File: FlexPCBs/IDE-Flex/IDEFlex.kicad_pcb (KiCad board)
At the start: 2 copper layers, 106.1 x 55.1 mm, 18 parts, among them J1 Conn_01x04_Pin, J2 Conn_01x04_Pin, J3 Conn_01x04_Pin, J4 Conn_01x04_Pin, J5 Conn_01x04_Pin, J6 Conn_01x04_Pin, J7 Conn_01x04_Pin, U1 IDE25

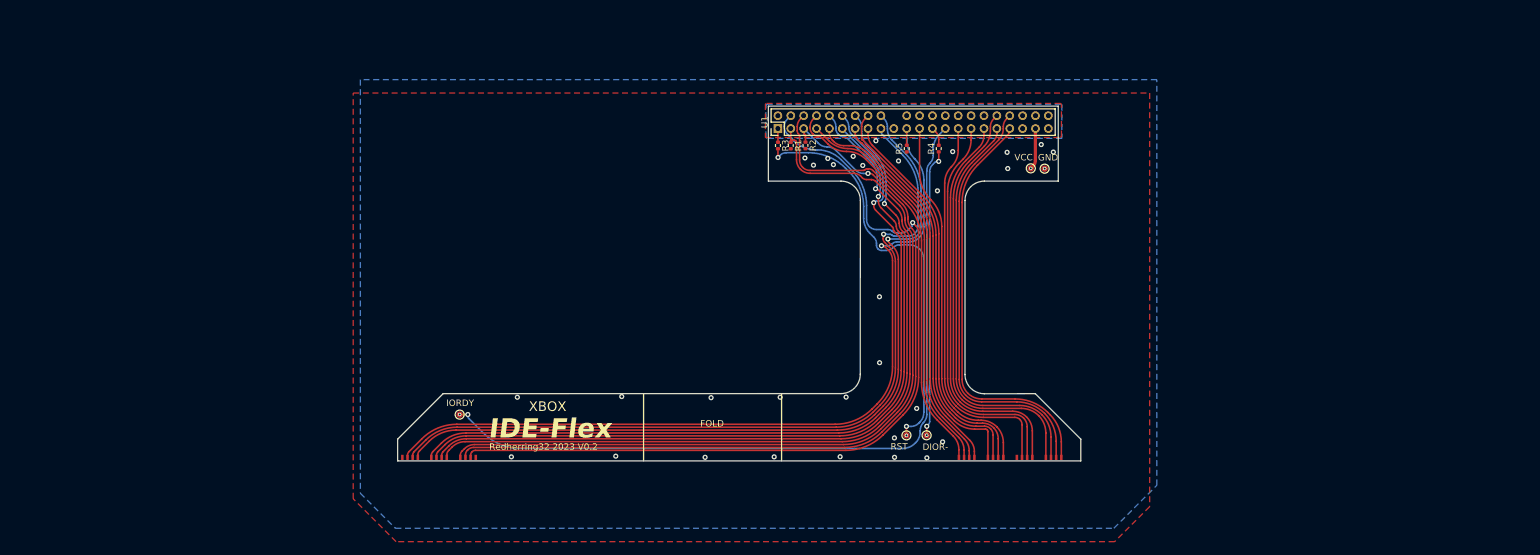
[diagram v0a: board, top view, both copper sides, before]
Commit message: Delete HDMI Flipper Design Add HDMI Flex Add USB C/Power and volume button PCB Add Housing CAD Update IDE Flex Update S Controller PCBs Update LPC Flex Update USB Flex
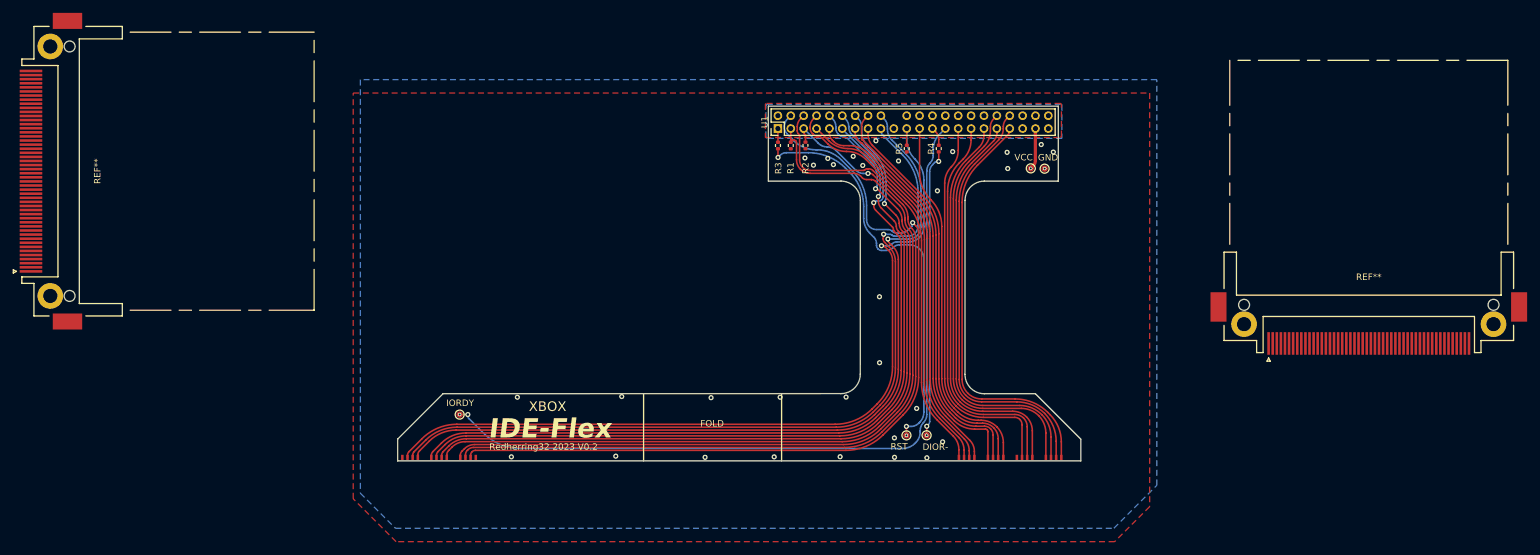
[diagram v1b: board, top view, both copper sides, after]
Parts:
- added REF**: CF-Card_3M_N7E50-E516xx-30, Connector_Card:CF-Card_3M_N7E50-E516xx-30, F.Cu at (51.3, 236.7)
- added REF**: CF-Card_3M_N7E50-A516xx-30, Connector_Card:CF-Card_3M_N7E50-A516xx-30, F.Cu at (256.0, 260.3)
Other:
- copper layers 2 -> 11
